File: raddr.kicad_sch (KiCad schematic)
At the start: 8 parts, among them J1 Conn_01x03, J2 Conn_01x01, J3 Conn_01x04, J4 Conn_01x01, U1 PMS150C-U06

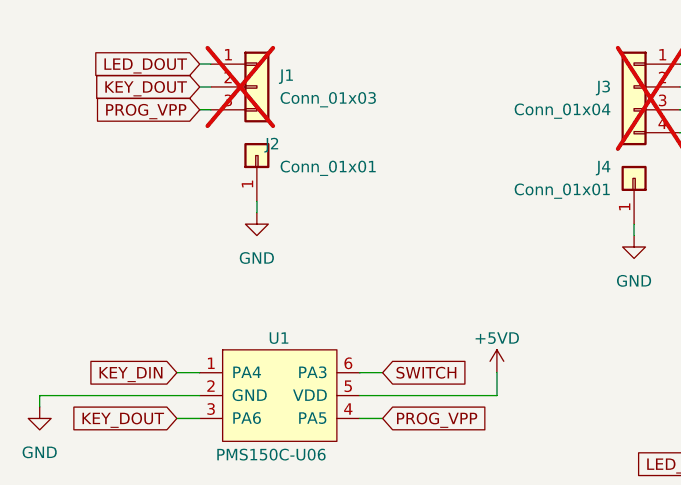
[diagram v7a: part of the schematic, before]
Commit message: overhaul
- Align on grid
- fillet
- shring X dim
- center button
- remove extra bttn holes
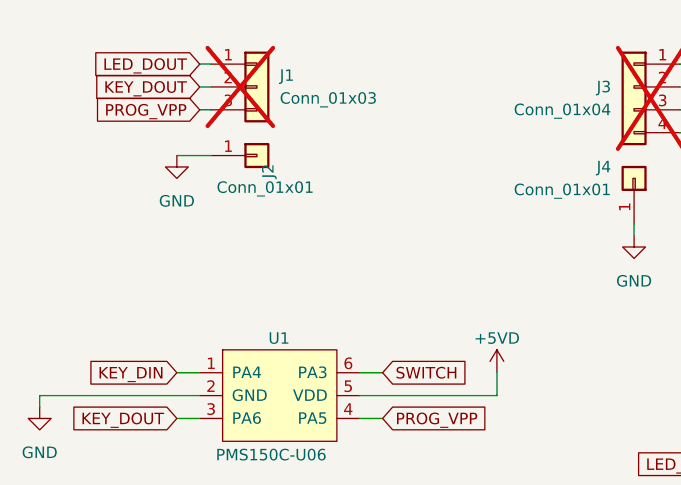
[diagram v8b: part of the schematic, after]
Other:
- moved on the sheet: J2
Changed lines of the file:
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@@
+	(wire
+		(pts
+			(xy 85.09 41.91) (xy 88.9 41.91)
+		)
+		(stroke
+			(width 0)
+			(type default)
+		)
+	)
 	(wire
 		(pts
@@
 		(pts
 			(xy 144.78 34.29) (xy 140.97 34.29)
-		)
-		(stroke
-			(width 0)
-			(type default)
-		)
-	)
-	(wire
-		(pts
-			(xy 93.98 46.99) (xy 93.98 48.26)
 		)
 		(stroke
@@
 	(symbol
 		(lib_id "Connector_Generic:Conn_01x01")
-		(at 93.98 41.91 90)
+		(at 93.98 41.91 0)
 		(unit 1)
 		(exclude_from_sim no)
@@
 		(dnp no)
 		(property "Reference" "J2"
-			(at 96.52 40.6399 90)
+			(at 95.2501 44.45 90)
 			(effects
 				(font
@@
 		)
 		(property "Value" "Conn_01x01"
-			(at 96.52 43.1799 90)
+			(at 100.3301 45.466 0)
 			(effects
 				(font
@@
 	(symbol
 		(lib_id "power:GND")
-		(at 93.98 48.26 0)
+		(at 85.09 41.91 0)
 		(unit 1)
 		(exclude_from_sim no)
@@
 		(fields_autoplaced yes)
 		(property "Reference" "#PWR02"
-			(at 93.98 54.61 0)
+			(at 85.09 48.26 0)
 			(effects
 				(font
@@
 		)
 		(property "Value" "GND"
-			(at 93.98 53.34 0)
+			(at 85.09 46.99 0)
 			(effects
 				(font
@@
 		)
 		(property "Footprint" ""
-			(at 93.98 48.26 0)
+			(at 85.09 41.91 0)
 			(effects
 				(font
@@
 		)
 		(property "Datasheet" ""
-			(at 93.98 48.26 0)
+			(at 85.09 41.91 0)
 			(effects
 				(font
@@
 		)
 		(property "Description" "Power symbol creates a global label with name \"GND\" , ground"
-			(at 93.98 48.26 0)
-			(effects
-				(font
-					(size 1.27 1.27)
-				)
-				(hide yes)
-			)
-		)
-		(pin "1"
-		)
-		(instances
-			(project "raddr"
+			(at 85.09 41.91 0)
+			(effects
+				(font
+					(size 1.27 1.27)
+				)
+				(hide yes)
+			)
+		)
+		(pin "1"
+		)
+		(instances
+			(project ""
 				(path "/9585471a-96c4-4019-bcf7-b3f1c776d0db"
 					(reference "#PWR02")
